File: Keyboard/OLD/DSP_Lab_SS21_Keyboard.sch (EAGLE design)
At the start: 13 parts, among them J1 640455-2

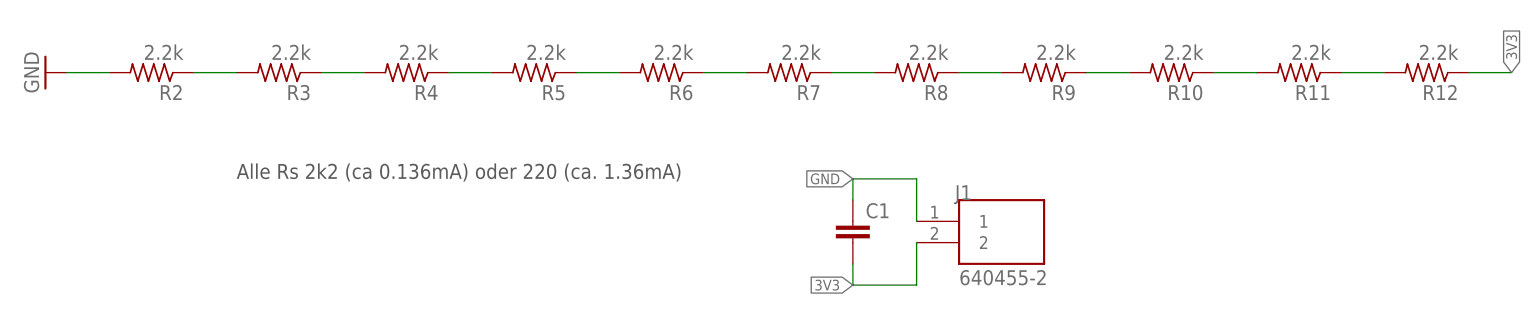
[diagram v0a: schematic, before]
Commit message: Keyboard pictures added and sch updated
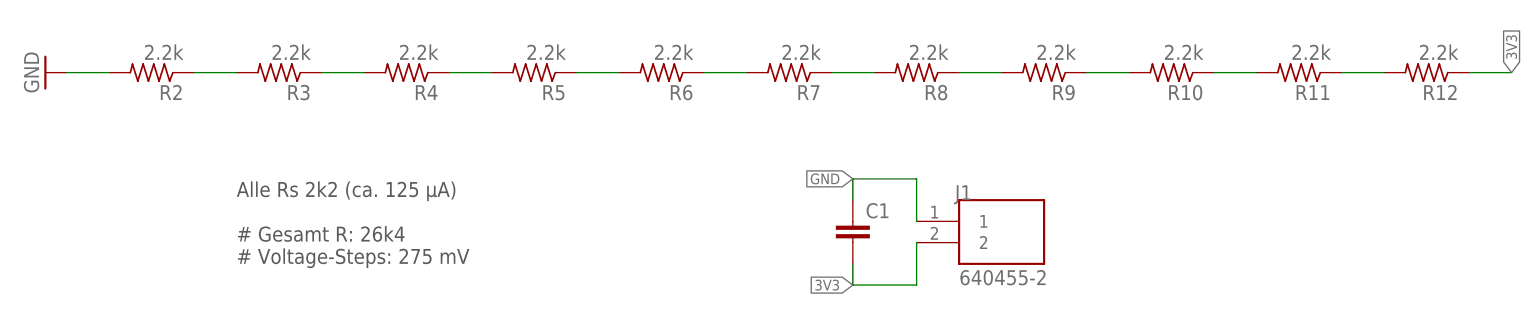
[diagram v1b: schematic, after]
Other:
- note added: "Alle Rs 2k2 (ca. 125 µA) # Gesamt R: 26k4 # Voltage-Steps: 275 mV"
- note removed: "Alle Rs 2k2 (ca 0.136mA) oder 220 (ca. 1.36mA)"
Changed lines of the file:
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@@
 <?xml version="1.0" encoding="utf-8"?>
 <!DOCTYPE eagle SYSTEM "eagle.dtd">
-<eagle version="9.5.2">
+<eagle version="9.6.2">
 <drawing>
 <settings>
@@
 <sheet>
 <plain>
-<text x="-55.88" y="7.62" size="1.778" layer="97">Alle Rs 2k2 (ca 0.136mA) oder 220 (ca. 1.36mA)</text>
+<text x="-55.88" y="-2.54" size="1.778" layer="97">Alle Rs 2k2 (ca. 125 µA)
+# Gesamt R: 26k4
+# Voltage-Steps: 275 mV</text>
 </plain>
 <instances>
@@
 </drawing>
 <compatibility>
+<note version="6.3" minversion="6.2.2" severity="warning">
+Since Version 6.2.2 text objects can contain more than one line,
+which will not be processed correctly with this version.
+</note>
 <note version="8.2" severity="warning">
 Since Version 8.2, EAGLE supports online libraries. The ids
